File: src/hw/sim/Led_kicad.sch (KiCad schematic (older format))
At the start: 11 parts, among them Q1 2N2222A, Q2 2N2222A

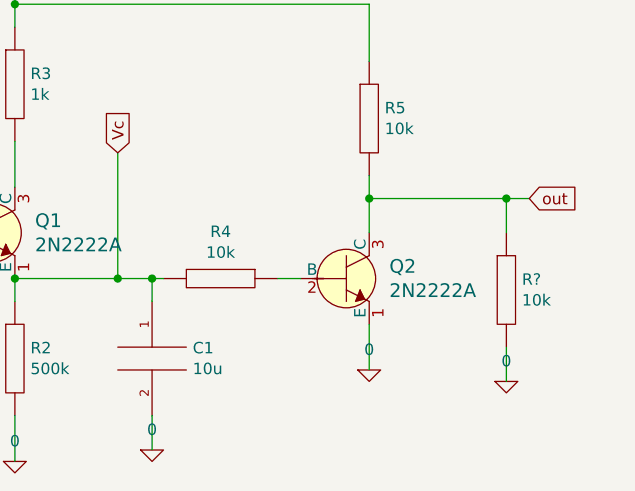
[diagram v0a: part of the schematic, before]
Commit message: tune lesvaleurs de C1 et R6 #27
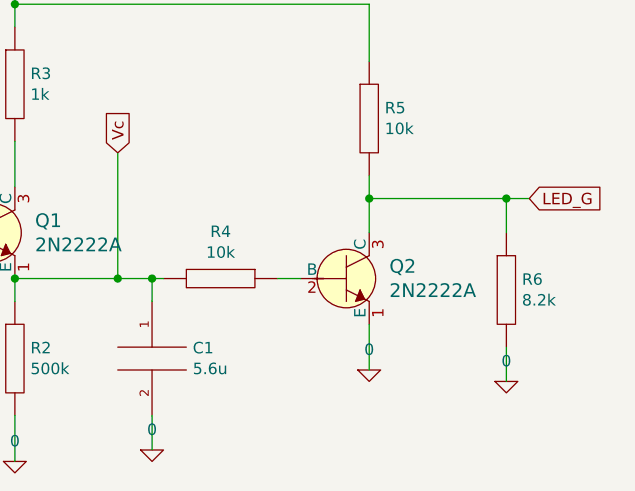
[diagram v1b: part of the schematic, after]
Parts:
- C1: value 10u -> 5.6u
- R6: renamed from R?; value 10k -> 8.2k
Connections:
- net labels added: LED_G
- net labels removed: out
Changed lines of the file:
@@
 	2050 2550 2050 2350
 Text GLabel 7150 2900 2    50   Input ~ 0
-out
+LED_G
 Wire Wire Line
 	4900 3850 4900 4050
@@
 P 5500 3600
 F 0 "C1" H 5678 3646 50  0000 L CNN
-F 1 "10u" H 5678 3555 50  0000 L CNN
+F 1 "5.6u" H 5678 3555 50  0000 L CNN
 F 2 "" H 5500 3600 50  0001 C CNN
 F 3 "~" H 5500 3600 50  0001 C CNN
@@
 	5350 3250 5500 3250
 $Comp
-L pspice:R R?
+L pspice:R R6
 U 1 1 5E7B8190
 P 7050 3300
-F 0 "R?" H 7118 3346 50  0000 L CNN
-F 1 "10k" H 7118 3255 50  0000 L CNN
+F 0 "R6" H 7118 3346 50  0000 L CNN
+F 1 "8.2k" H 7118 3255 50  0000 L CNN
 F 2 "" H 7050 3300 50  0001 C CNN
 F 3 "~" H 7050 3300 50  0001 C CNN

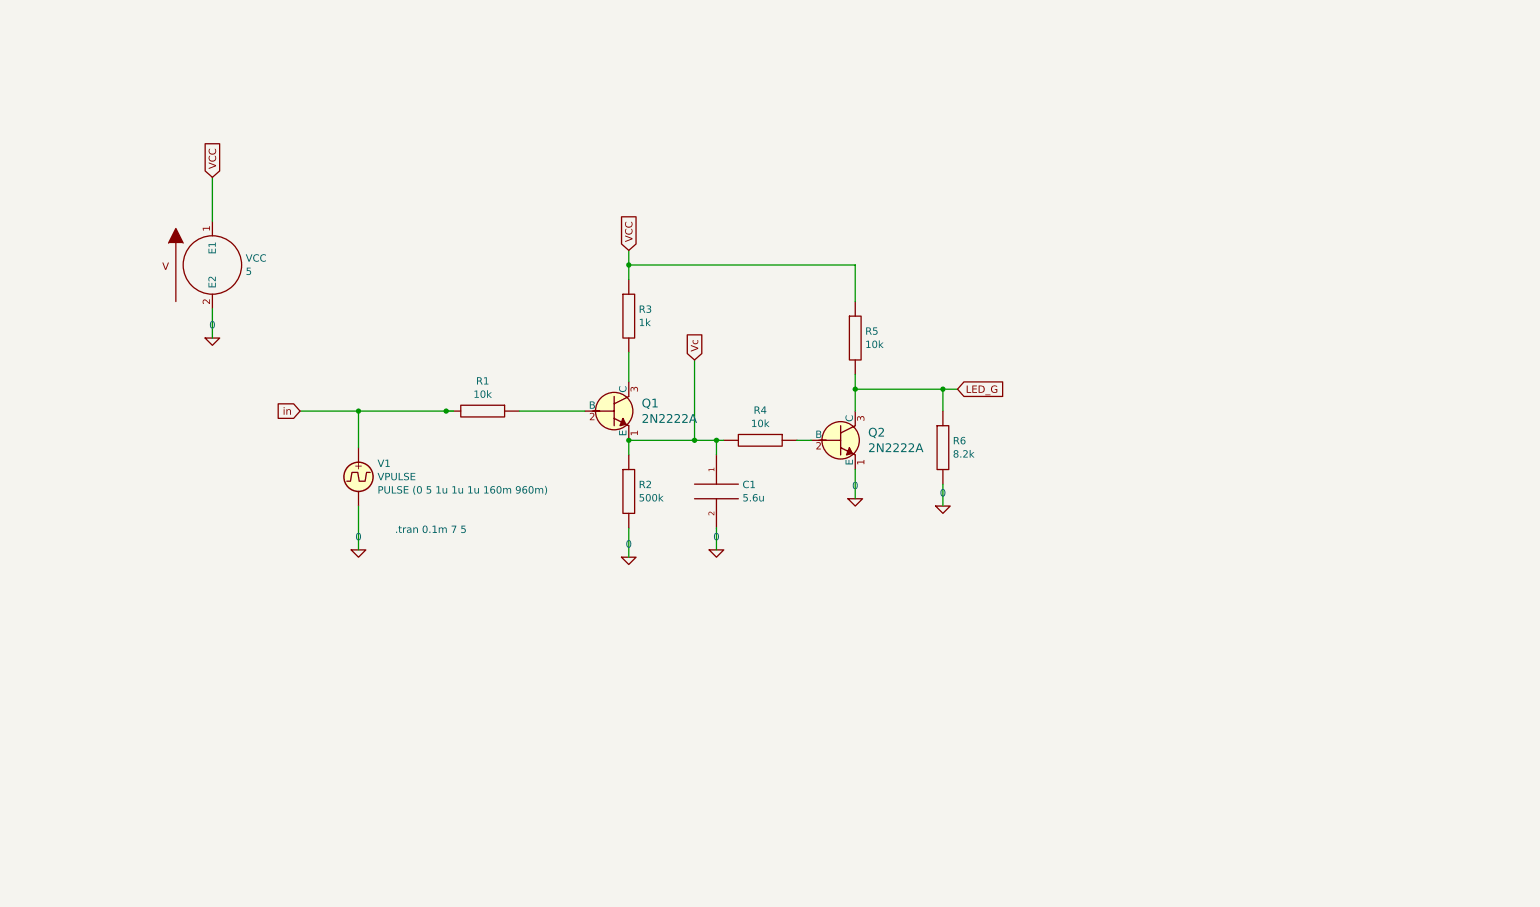
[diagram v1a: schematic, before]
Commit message: ajout de l'état "Batterie chargée" #27
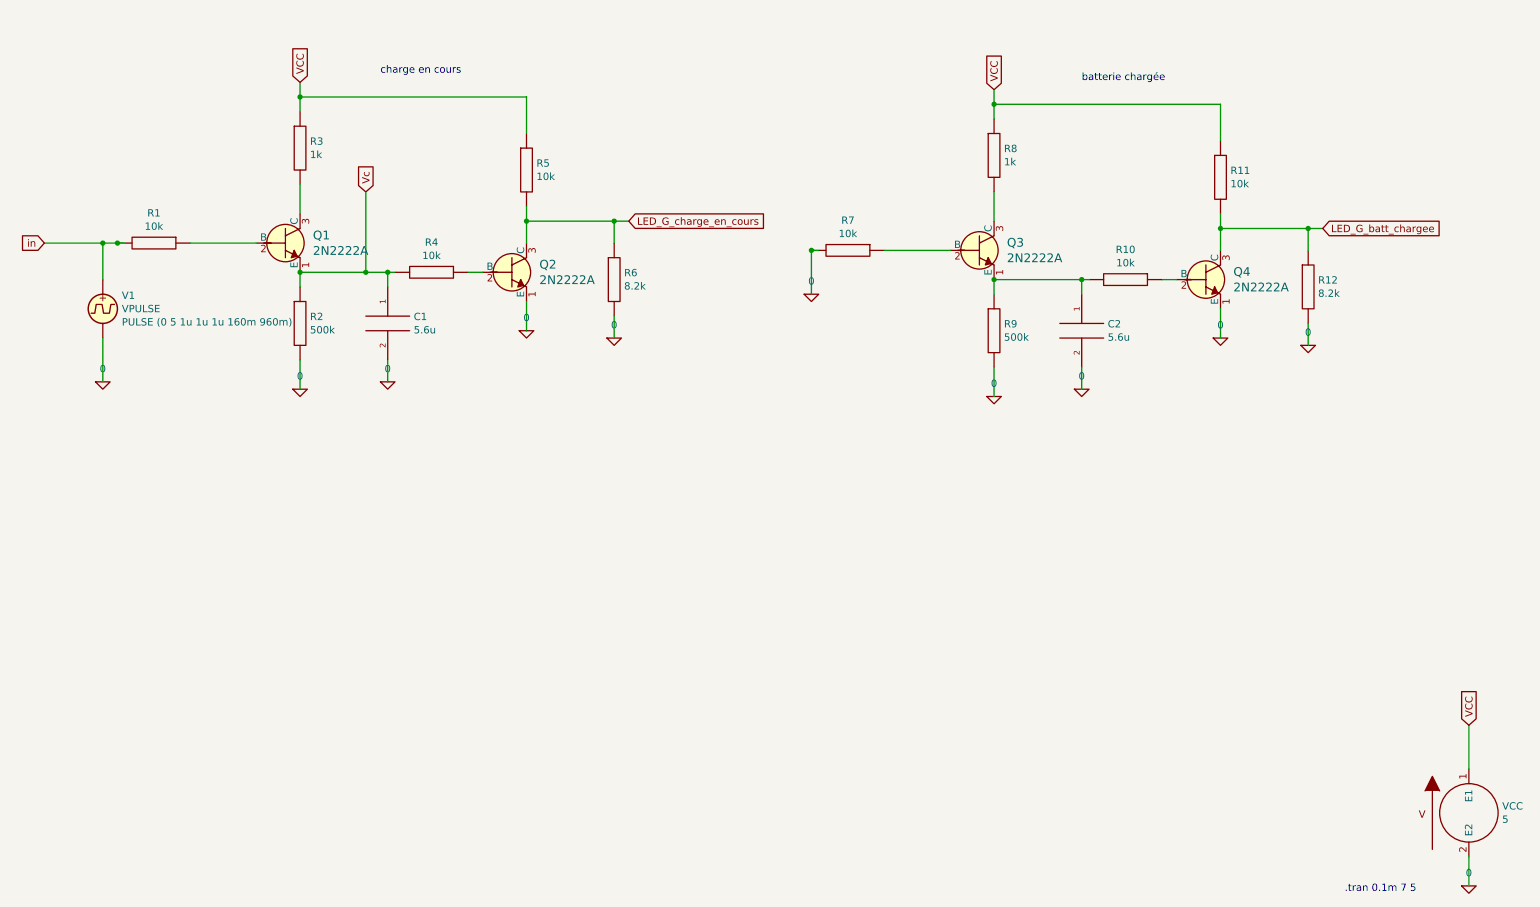
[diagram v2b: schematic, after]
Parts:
- added C2: 5.6u, symbol pspice:C
- added Q3, Q4: 2N2222A, digikey-footprints:TO-18-3, symbol dk_Transistors-Bipolar-BJT-Single:2N2222A
- added R10, R11, R7: 10k, symbol pspice:R
- added R12: 8.2k, symbol pspice:R
- added R8: 1k, symbol pspice:R
- added R9: 500k, symbol pspice:R
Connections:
- net labels added: LED_G_batt_chargee, LED_G_charge_en_cours
- net labels removed: LED_G
- wire segments 29 -> 51
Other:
- note added: "batterie chargée"
- note added: "charge en cours"
- moved on the sheet: C1, Q1, Q2, R1, R2, R3, R4, R5, R6, V1, VCC

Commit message: c'est la crise du logement... #27
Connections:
- wire segments 51 -> 50
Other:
- moved on the sheet: C1, C2, Q1, Q2, Q3, Q4, R1, R10, R11, R12, R2, R3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

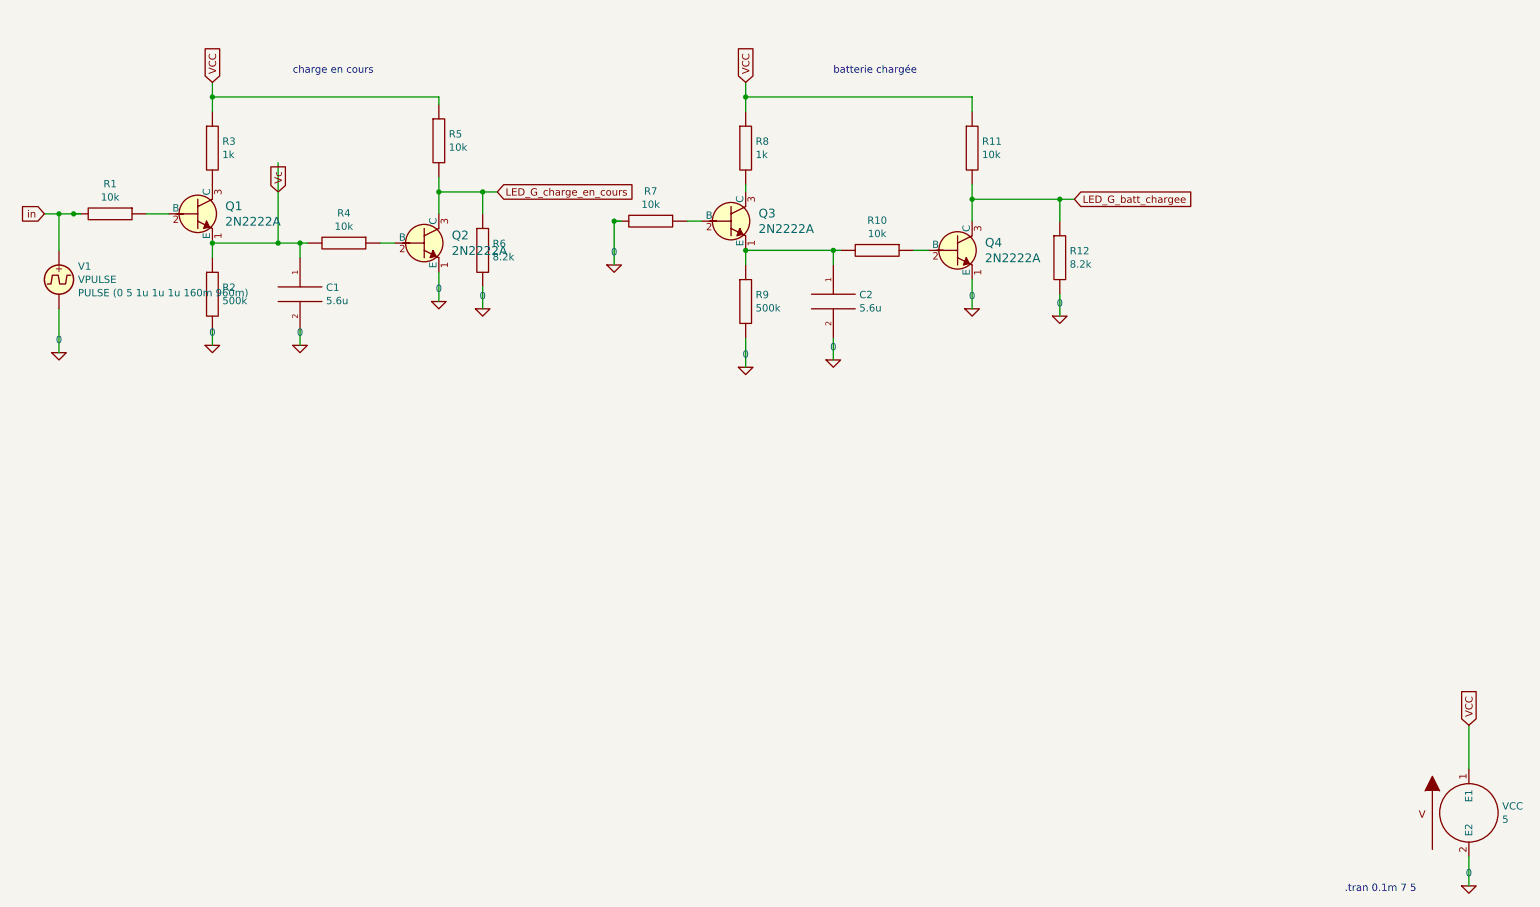
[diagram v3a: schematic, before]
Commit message: etat "batterie erreur"
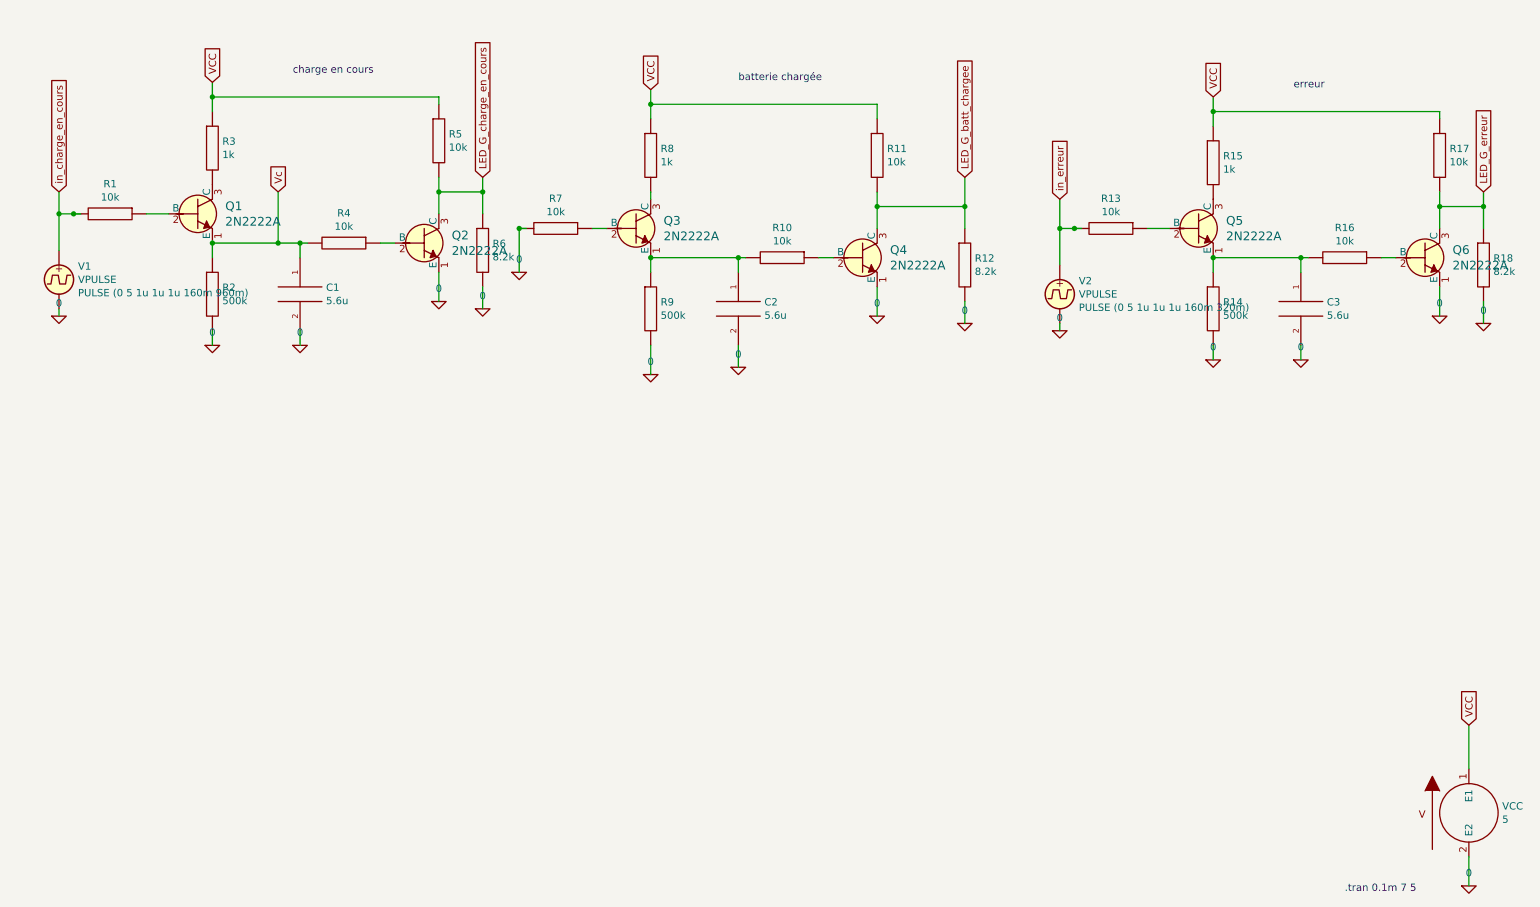
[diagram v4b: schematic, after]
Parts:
- added C3: 5.6u, symbol pspice:C
- added Q5, Q6: 2N2222A, digikey-footprints:TO-18-3, symbol dk_Transistors-Bipolar-BJT-Single:2N2222A
- added R13, R16, R17: 10k, symbol pspice:R
- added R14: 500k, symbol pspice:R
- added R15: 1k, symbol pspice:R
- added R18: 8.2k, symbol pspice:R
- added V2: VPULSE, symbol Simulation_SPICE:VPULSE
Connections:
- net labels added: LED_G_erreur, in_charge_en_cours, in_erreur
- net labels removed: in
- wire segments 50 -> 74
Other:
- note added: "erreur"
- moved on the sheet: C2, Q3, Q4, R10, R11, R12, R7, R8, R9

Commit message: etat "batterie absente" #27
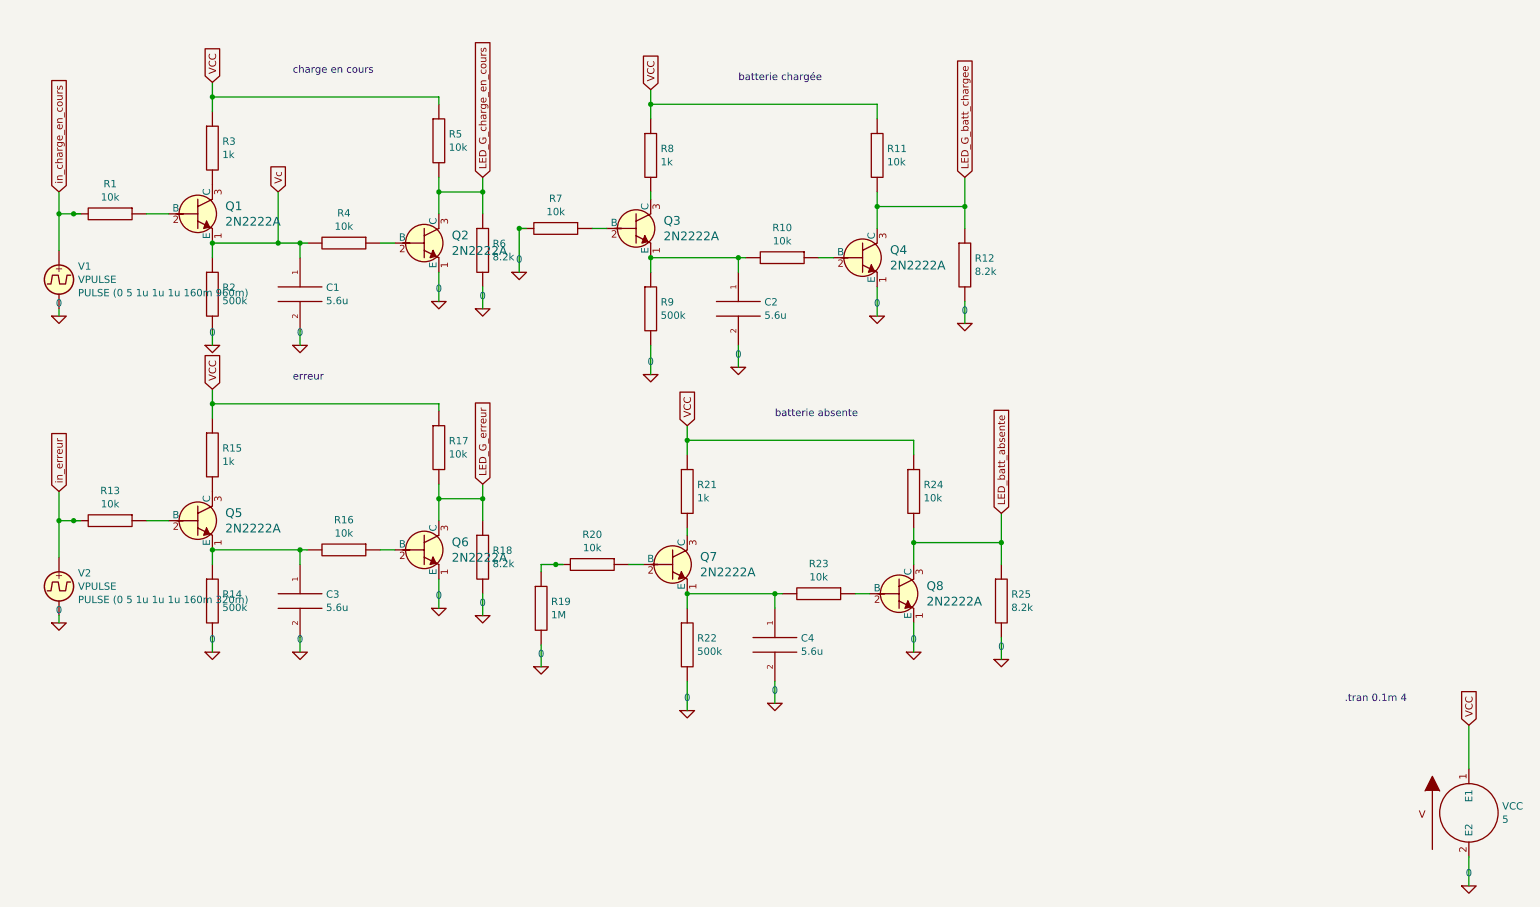
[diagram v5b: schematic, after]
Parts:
- added C4: 5.6u, symbol pspice:C
- added Q7, Q8: 2N2222A, digikey-footprints:TO-18-3, symbol dk_Transistors-Bipolar-BJT-Single:2N2222A
- added R19: 1M, symbol pspice:R
- added R20, R23, R24: 10k, symbol pspice:R
- added R21: 1k, symbol pspice:R
- added R22: 500k, symbol pspice:R
- added R25: 8.2k, symbol pspice:R
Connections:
- net labels added: LED_batt_absente
- wire segments 74 -> 98
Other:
- note added: ".tran 0.1m 4"
- note added: "batterie absente"
- note removed: ".tran 0.1m 7 5"
- moved on the sheet: C3, Q5, Q6, R13, R14, R15, R16, R17, R18, V2
